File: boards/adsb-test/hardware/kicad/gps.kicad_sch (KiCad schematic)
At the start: 0 parts

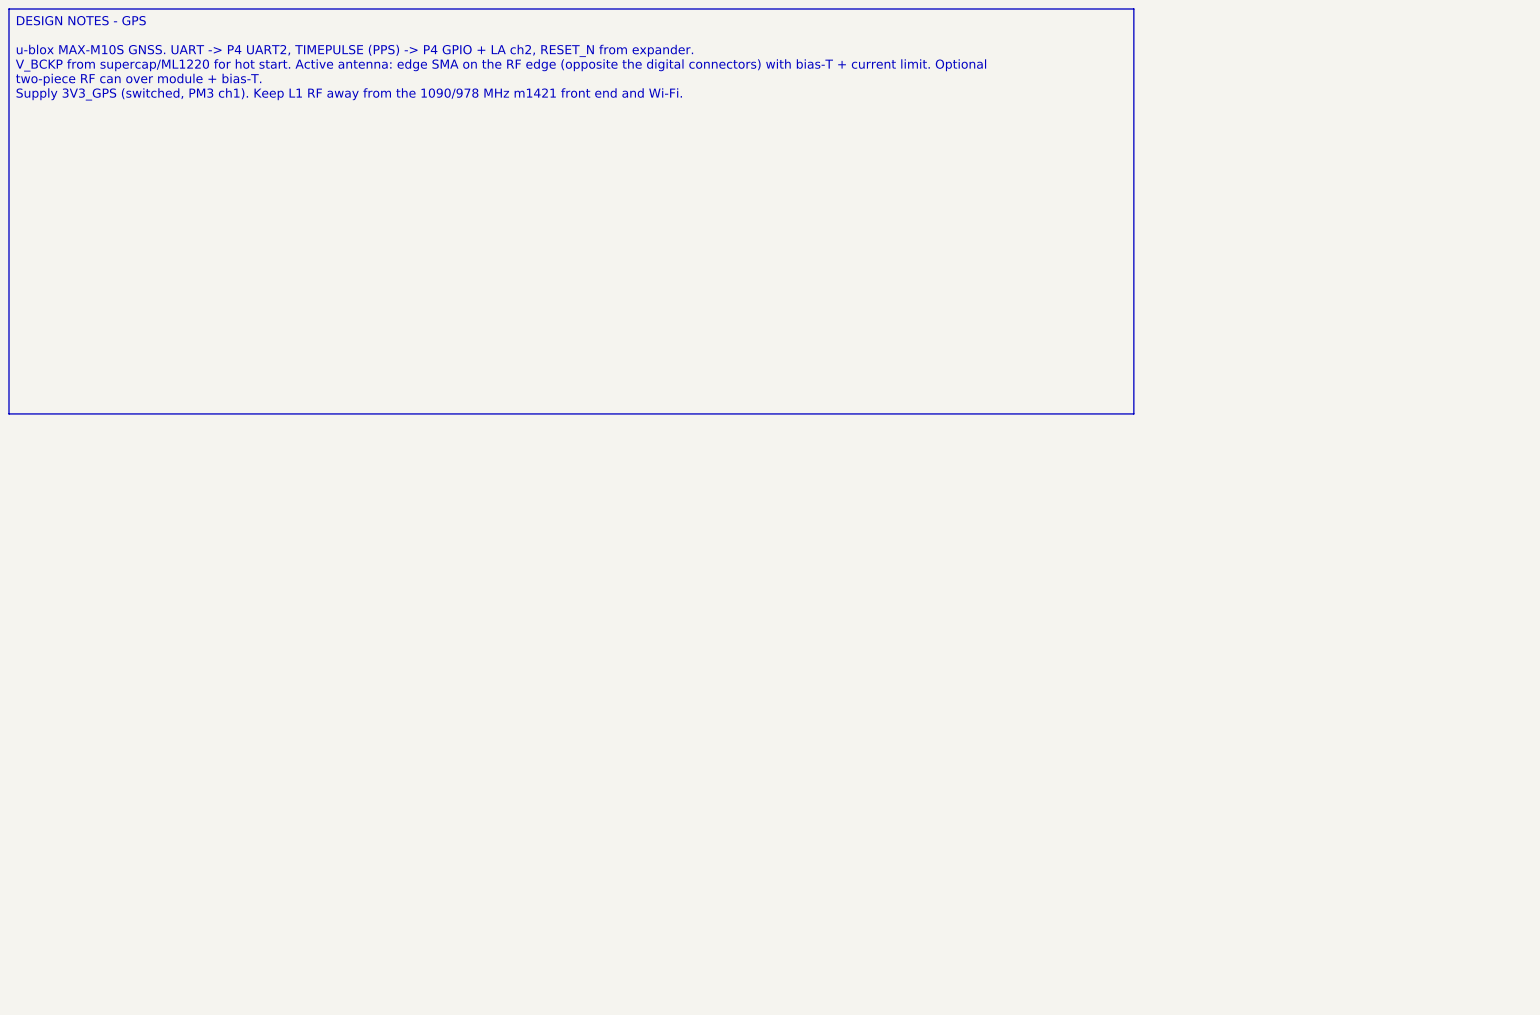
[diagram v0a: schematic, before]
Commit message: Release v0.22.0: all ADSB_Test schematic sheets generated (ERC clean)
Co-Authored-By: Claude Opus 5.5 <noreply@anthropic.com>
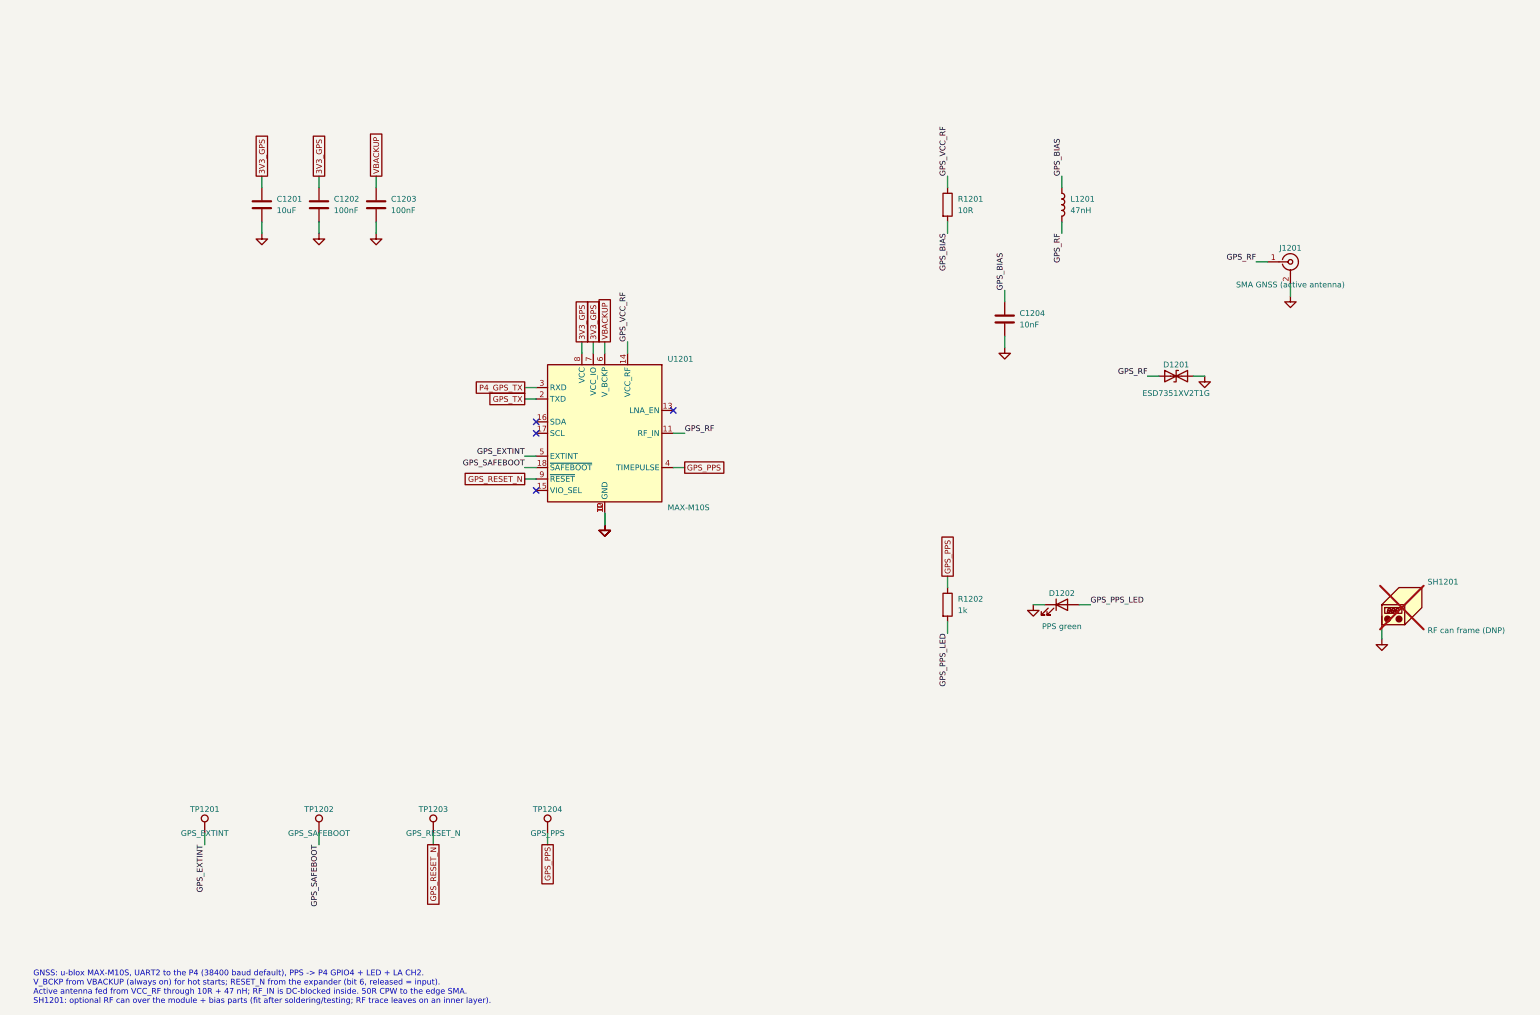
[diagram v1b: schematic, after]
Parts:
- added C1201: 10uF, Capacitor_SMD:C_1206_3216Metric_Pad1.33x1.80mm_HandSolder, symbol Device:C
- added C1202, C1203: 100nF, Capacitor_SMD:C_0805_2012Metric_Pad1.18x1.45mm_HandSolder, symbol Device:C
- added C1204: 10nF, Capacitor_SMD:C_0805_2012Metric_Pad1.18x1.45mm_HandSolder, symbol Device:C
- added D1201: ESD7351XV2T1G, Diode_SMD:D_SOD-523, symbol Device:D_TVS
- added D1202: PPS green, LED_SMD:LED_0805_2012Metric_Pad1.15x1.40mm_HandSolder, symbol Device:LED
- added J1201: SMA GNSS (active antenna), Connector_Coaxial:SMA_Samtec_SMA-J-P-H-ST-EM1_EdgeMount, symbol Connector:Conn_Coaxial
- added L1201: 47nH, Inductor_SMD:L_0805_2012Metric_Pad1.05x1.20mm_HandSolder, symbol Device:L
- added R1201: 10R, Resistor_SMD:R_0805_2012Metric_Pad1.20x1.40mm_HandSolder, symbol Device:R
- added R1202: 1k, Resistor_SMD:R_0805_2012Metric_Pad1.20x1.40mm_HandSolder, symbol Device:R
- added SH1201: RF can frame (DNP), RF_Shielding:Laird_Technologies_BMI-S-202-F_16.50x16.50mm, symbol Mechanical:Housing_Pad
- added TP1201: GPS_EXTINT, TestPoint:TestPoint_Pad_D1.5mm, symbol Connector:TestPoint
- added TP1202: GPS_SAFEBOOT, TestPoint:TestPoint_Pad_D1.5mm, symbol Connector:TestPoint
- added TP1203: GPS_RESET_N, TestPoint:TestPoint_Pad_D1.5mm, symbol Connector:TestPoint
- added TP1204: GPS_PPS, TestPoint:TestPoint_Pad_D1.5mm, symbol Connector:TestPoint
- added U1201: MAX-M10S, RF_GPS:ublox_MAX, symbol RF_GPS:MAX-M10S
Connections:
- new net 3V3_GPS: C1201.1, C1202.1, U1201.7 (VCC_IO), U1201.8 (VCC)
- new net GND: C1201.2, C1202.2, C1203.2, C1204.2, D1201.2 (A2), D1202.1 (K), J1201.2 (Ext), SH1201.1 (PAD), U1201.1 (GND), U1201.10 (GND), U1201.12 (GND)
- new net GPS_BIAS: C1204.1, L1201.1, R1201.2
- new net GPS_EXTINT: TP1201.1, U1201.5 (EXTINT)
- new net GPS_PPS: R1202.1, TP1204.1, U1201.4 (TIMEPULSE)
- new net GPS_PPS_LED: D1202.2 (A), R1202.2
- new net GPS_RESET_N: TP1203.1, U1201.9 (~{RESET})
- new net GPS_RF: D1201.1 (A1), J1201.1 (In), L1201.2, U1201.11 (RF_IN)
- new net GPS_SAFEBOOT: TP1202.1, U1201.18 (~{SAFEBOOT})
- new net GPS_TX: U1201.2 (TXD)
- new net GPS_VCC_RF: R1201.1, U1201.14 (VCC_RF)
- new net P4_GPS_TX: U1201.3 (RXD)
- new net VBACKUP: C1203.1, U1201.6 (V_BCKP)
- no-connect marks 0 -> 4
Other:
- note added: "GNSS: u-blox MAX-M10S, UART2 to the P4 (38400 baud default), PPS -> P4 GPIO4 + LED + LA CH2. V_BCKP from VBACKUP (always on) for hot starts; RESET_N from the expander (bit 6, released = input). Active antenna fed from VCC_RF through 10R + 47 nH; RF_IN is DC-blocked inside. 50R CPW to the edge SMA. SH1201: optional RF can over the module + bias parts (fit after soldering/testing; RF trace leaves o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"

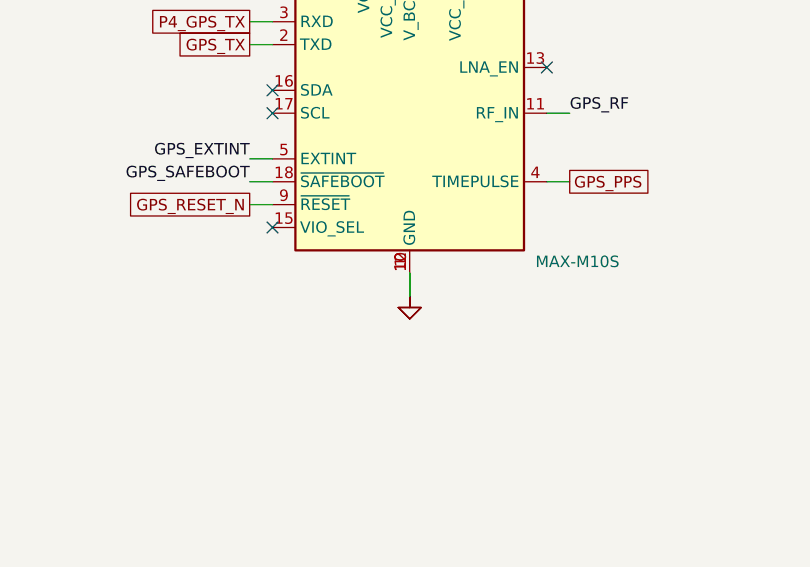
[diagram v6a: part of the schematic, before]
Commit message: Schematic generator: hide stacked pins (KiCad convention) so pin numbers don't overprint
Co-Authored-By: Claude Opus 5.5 <noreply@anthropic.com>
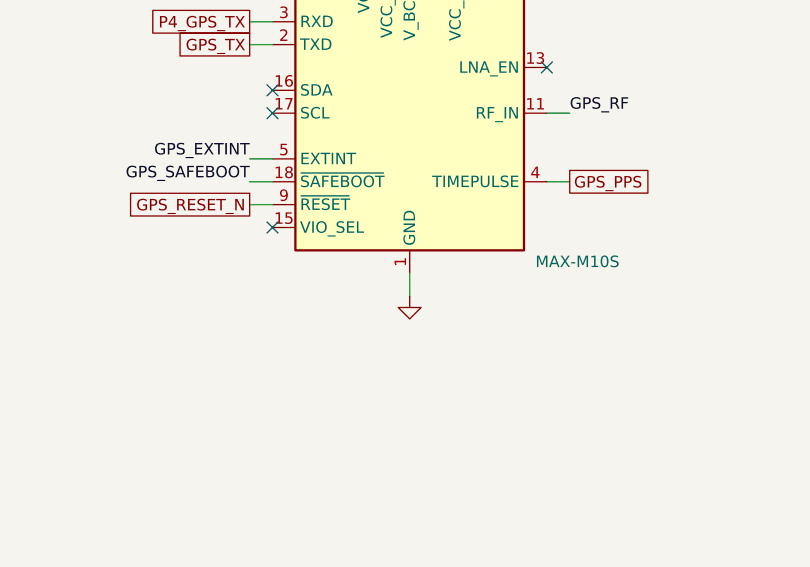
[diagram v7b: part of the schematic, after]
